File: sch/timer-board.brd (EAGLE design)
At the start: 76.2 x 69.9 mm, 35 parts, among them IC1 ATMEGA328P

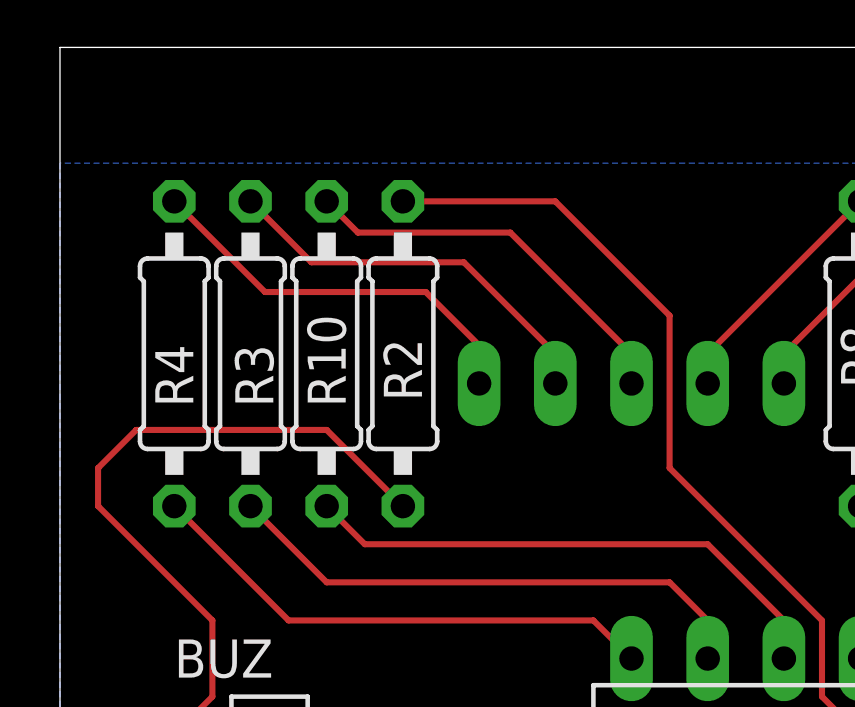
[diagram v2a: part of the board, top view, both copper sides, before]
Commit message: PCB : Fixed resistor label
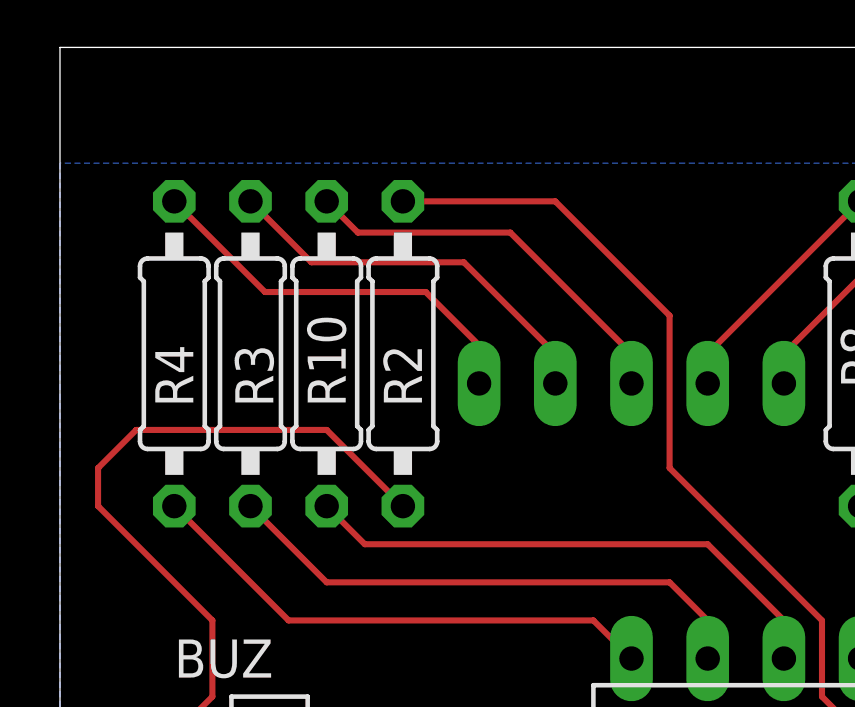
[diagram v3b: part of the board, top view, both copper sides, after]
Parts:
- turned R2 to 90 degrees
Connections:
- net BUZ: now also R2.2; no longer R2.1
- net N$8: now also R2.1; no longer R2.2
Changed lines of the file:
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@@
 <attribute name="SPICEPREFIX" value="R" x="31.75" y="59.69" size="1.778" layer="27" rot="R90" display="off"/>
-</element>
-<element name="R2" library="rcl" library_urn="urn:adsk.eagle:library:334" package="0207/10" package3d_urn="urn:adsk.eagle:package:23491/1" value="" x="11.43" y="59.69" smashed="yes" rot="R270">
-<attribute name="NAME" x="10.795" y="60.198" size="1.27" layer="25" ratio="10" rot="R270"/>
-<attribute name="SPICEPREFIX" value="R" x="11.43" y="59.69" size="1.778" layer="27" rot="R270" display="off"/>
-<attribute name="VALUE" x="10.795" y="61.9506" size="1.27" layer="27" ratio="10" rot="R270"/>
 </element>
 <element name="C5" library="rcl" library_urn="urn:adsk.eagle:library:334" package="E2,5-6" package3d_urn="urn:adsk.eagle:package:23349/1" value="100uF" x="58.42" y="46.99" smashed="yes" rot="R90">
@@
 <element name="LOGO1" library="SparkFun-Aesthetics" library_urn="urn:adsk.eagle:library:507" package="OSHW-LOGO-L_COPPER" package3d_urn="urn:adsk.eagle:package:37117/1" value="OSHW-LOGOL-COPPER" x="44.45" y="11.43"/>
 <element name="U$1" library="parts" package="DOG" value="DOG_LOGO" x="8.89" y="15.24"/>
+<element name="R2" library="rcl" library_urn="urn:adsk.eagle:library:334" package="0207/10" package3d_urn="urn:adsk.eagle:package:23491/1" value="" x="11.43" y="59.69" smashed="yes" rot="R90">
+<attribute name="NAME" x="12.065" y="57.912" size="1.27" layer="25" ratio="10" rot="R90"/>
+<attribute name="SPICEPREFIX" value="R" x="11.43" y="59.69" size="1.778" layer="27" rot="R90" display="off"/>
+<attribute name="VALUE" x="12.065" y="57.4294" size="1.27" layer="27" ratio="10" rot="R90"/>
+</element>
 </elements>
 <signals>
@@
 <signal name="BUZ">
 <contactref element="IC1" pad="23"/>
-<contactref element="R2" pad="1"/>
-<wire x1="11.43" y1="64.77" x2="16.51" y2="64.77" width="0.2032" layer="1"/>
 <wire x1="16.51" y1="64.77" x2="20.32" y2="60.96" width="0.2032" layer="1"/>
 <wire x1="20.32" y1="60.96" x2="20.32" y2="55.88" width="0.2032" layer="1"/>
@@
 <via x="31.75" y="46.99" extent="1-16" drill="0.508"/>
 <wire x1="31.75" y1="46.99" x2="31.75" y2="49.53" width="0.2032" layer="1"/>
+<contactref element="R2" pad="2"/>
+<wire x1="11.43" y1="64.77" x2="16.51" y2="64.77" width="0.2032" layer="1"/>
 </signal>
 <signal name="XTAL1">
@@
 </signal>
 <signal name="N$8">
-<contactref element="R2" pad="2"/>
 <contactref element="BUZ" pad="1"/>
-<wire x1="11.43" y1="54.61" x2="8.89" y2="57.15" width="0.2032" layer="1"/>
 <wire x1="5.08" y1="50.8" x2="5.08" y2="48.26" width="0.2032" layer="1"/>
 <wire x1="2.54" y1="57.15" x2="1.27" y2="55.88" width="0.2032" layer="1"/>
@@
 <wire x1="8.89" y1="57.15" x2="2.54" y2="57.15" width="0.2032" layer="1"/>
 <wire x1="5.08" y1="48.26" x2="3.81" y2="46.99" width="0.2032" layer="1"/>
+<contactref element="R2" pad="1"/>
+<wire x1="11.43" y1="54.61" x2="8.89" y2="57.15" width="0.2032" layer="1"/>
 </signal>
 <signal name="VIN">

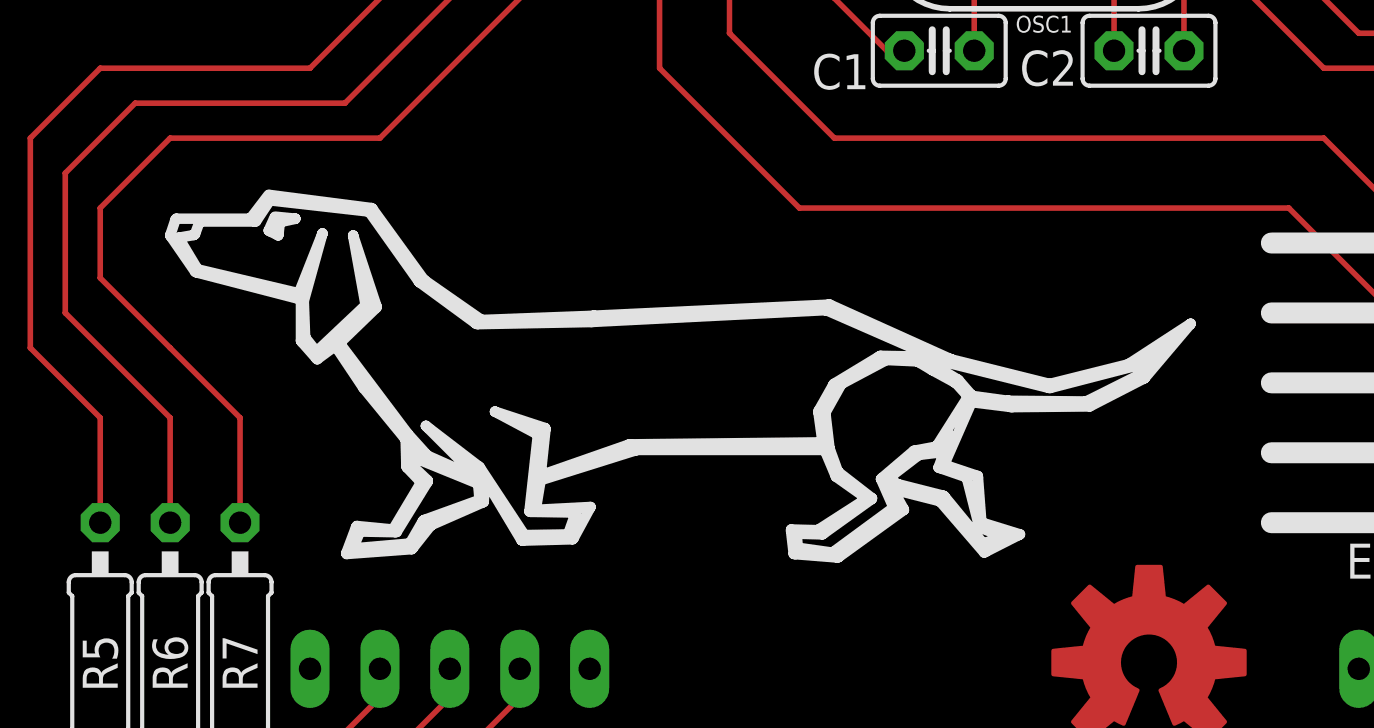
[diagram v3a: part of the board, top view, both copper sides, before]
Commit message: PCB : Updated dog logo
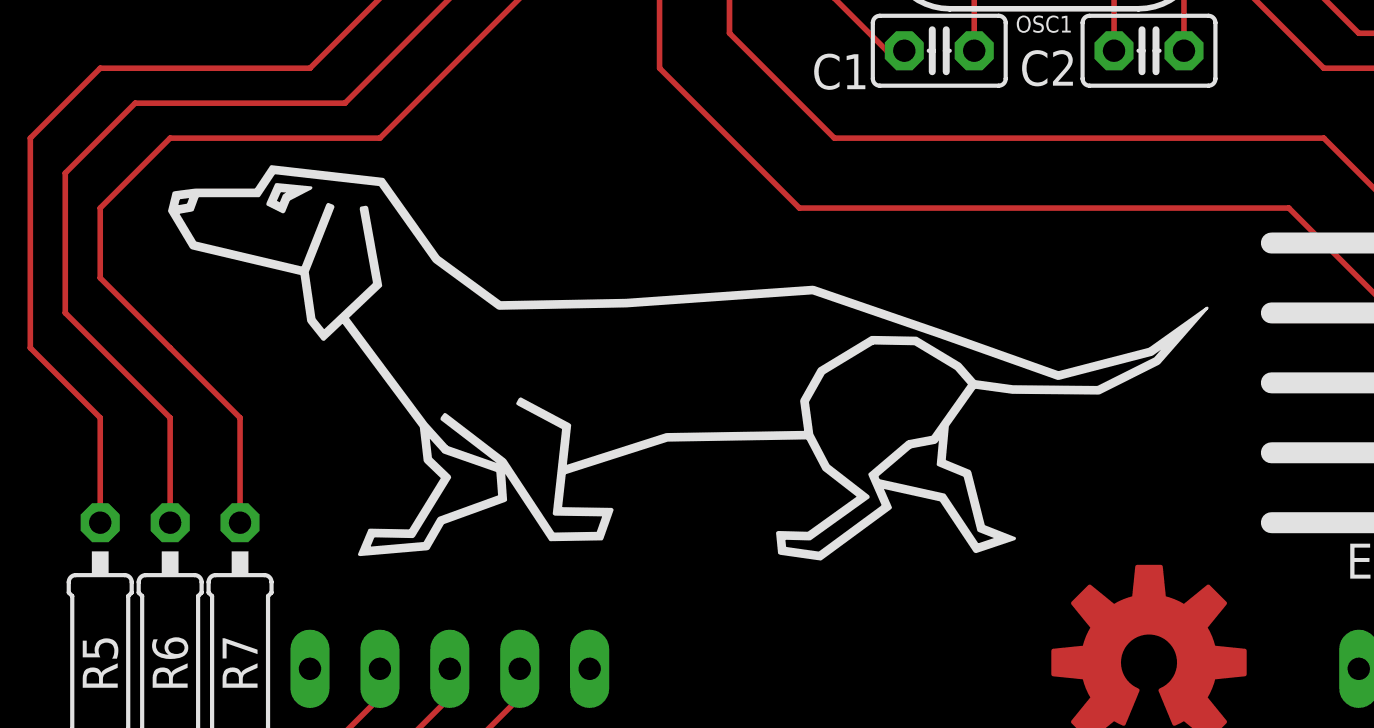
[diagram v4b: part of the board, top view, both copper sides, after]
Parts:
- U$1: value DOG_LOGO -> LOGO_DOG; device parts:DOG -> parts:LOGO_DOG
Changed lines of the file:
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@@
 </element>
 <element name="LOGO1" library="SparkFun-Aesthetics" library_urn="urn:adsk.eagle:library:507" package="OSHW-LOGO-L_COPPER" package3d_urn="urn:adsk.eagle:package:37117/1" value="OSHW-LOGOL-COPPER" x="44.45" y="11.43"/>
-<element name="U$1" library="parts" package="DOG" value="DOG_LOGO" x="8.89" y="15.24"/>
+<element name="U$1" library="parts" package="LOGO_DOG" value="LOGO_DOG" x="8.89" y="15.24"/>
 <element name="R2" library="rcl" library_urn="urn:adsk.eagle:library:334" package="0207/10" package3d_urn="urn:adsk.eagle:package:23491/1" value="" x="11.43" y="59.69" smashed="yes" rot="R90">
 <attribute name="NAME" x="12.065" y="57.912" size="1.27" layer="25" ratio="10" rot="R90"/>

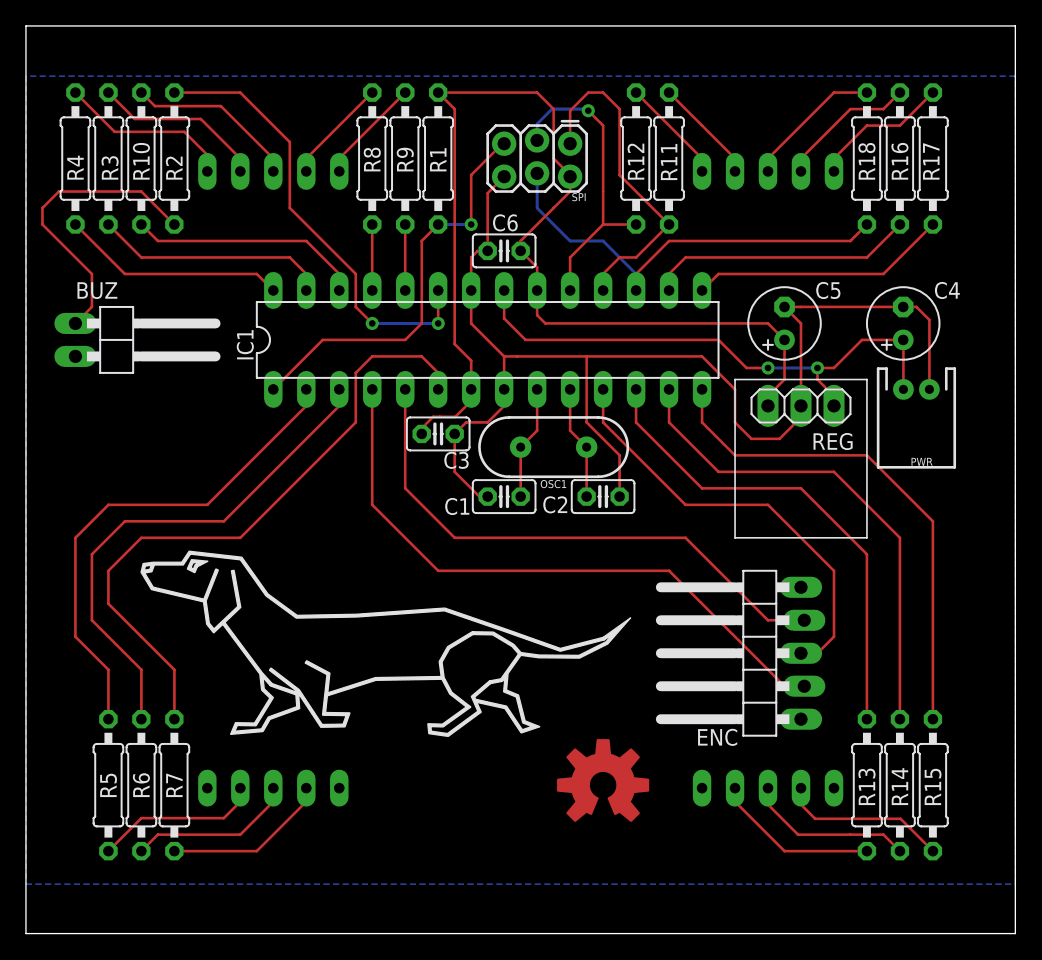
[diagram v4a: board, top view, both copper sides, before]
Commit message: feat: updated board to smaller layout
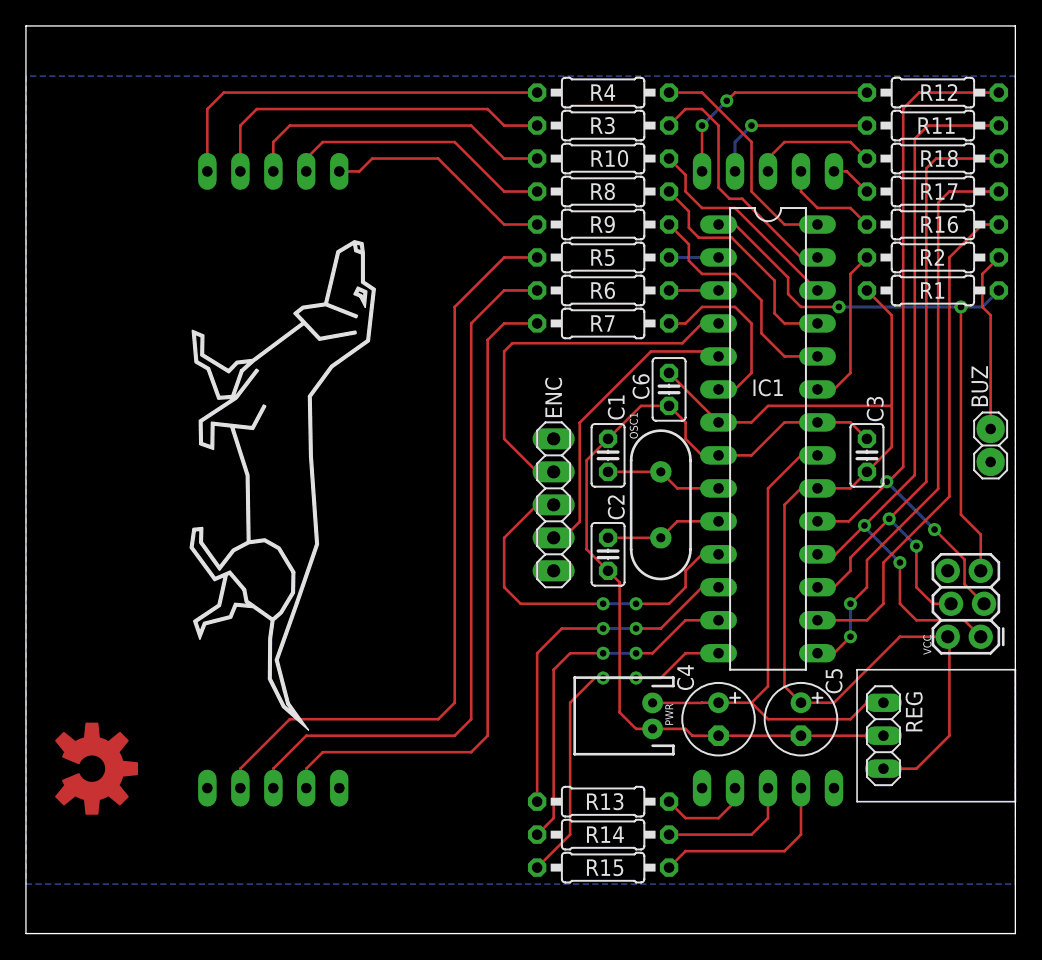
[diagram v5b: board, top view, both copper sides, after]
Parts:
- removed SPI: (no value), SparkFun-Connectors:2X3_LOCK
- added VCC: (no value), SparkFun-Connectors:2X3_LOCK
- BUZ: value (none) -> CONN_1X2; device pinhead:1X02/90 -> parts:CONN_1X2
- ENC: value (none) -> CONN_1X5CONN_1X5; device parts:1X5_ANGLE -> parts:CONN_1X5
- REG: value (none) -> VREG_STEP_UP
- moved BUZ 67.3 mm to (74.3, 36.3)
- moved R2 58.9 mm to (69.8, 52.1), turned to 180 degrees
- moved R5 55.7 mm to (44.5, 52.1), turned to 180 degrees
- moved R6 52.1 mm to (44.5, 49.5), turned to 180 degrees
- moved R7 48.5 mm to (44.5, 47.0), turned to 180 degrees
- moved R4 41.0 mm to (44.5, 64.8), turned to 180 degrees
- moved R1 39.4 mm to (69.8, 49.5), turned to 180 degrees
- moved LOGO1 39.4 mm to (5.08, 12.7), turned to 270 degrees
- moved U$1 38.3 mm to (12.7, 53.3), turned to 270 degrees
- moved R3 38.2 mm to (44.5, 62.2), turned to 180 degrees
- moved R10 35.6 mm to (44.5, 59.7), turned to 180 degrees
- moved C4 33.6 mm to (53.3, 16.5), turned to 270 degrees
- moved C3 33.1 mm to (64.8, 36.8), turned to 90 degrees
- moved PWR 32.3 mm to (48.3, 16.8), turned to 90 degrees
- moved C5 30.5 mm to (59.7, 16.5), turned to 270 degrees
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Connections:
- net D0A: now also VCC.1; no longer SPI.1
- net D0B: now also VCC.3; no longer SPI.3
- net D0P: now also VCC.4; no longer SPI.4
- net GND: now also VCC.6; no longer SPI.6
- net RST: now also VCC.5; no longer SPI.5
- net VCC: now also VCC.2; no longer SPI.2
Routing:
- net N$3: track 12.8 -> 58.5 mm
- net N$4: track 12.8 -> 54.9 mm
- net N$5: track 12.8 -> 51.3 mm
- net D1E: track 49.8 -> 14.3 mm
- net D1D: track 39.3 -> 3.81 mm
- net D1C: track 38.3 -> 3.81 mm
- net D0B: track 23.6 -> 56.6 mm, vias 1 -> 2
- net D0A: track 25.9 -> 57.3 mm, vias 0 -> 2
- net GND: track 96.6 -> 68.8 mm
- net D0G: track 19.9 -> 44.3 mm, vias 0 -> 2
- net BUZ: track 34.7 -> 12.5 mm, vias 2 -> 0
- net ENC1: track 42.6 -> 23.3 mm
- net ENC2: track 48.0 -> 29.0 mm
- net D0F: track 20.6 -> 39.2 mm
- net D0P: track 34.3 -> 51.7 mm, vias 0 -> 2
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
